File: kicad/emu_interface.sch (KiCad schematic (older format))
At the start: 19 parts

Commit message: power.sch added with new power 1V2, 3V3, an so global labels
I've added the power schematic and try to ojin the power label as 3V3,
VDD_3V3 an so.. keep going
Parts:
- C501, C504: renamed from C?; value ~ -> 4.7uF
- C503: renamed from C?; value ~ -> 0.01uF
- D502: renamed from D?; value ~ -> red
- D503: renamed from D?; value ~ -> blue
- D504: renamed from D?; value ~ -> green
- R501: renamed from R?; value ~ -> 680
- R502, R503: renamed from R?; value ~ -> 1.0k
- gave numbers to parts that had none: 10
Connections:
- net labels added: VDD_3V3
- net labels removed: VDD3V3

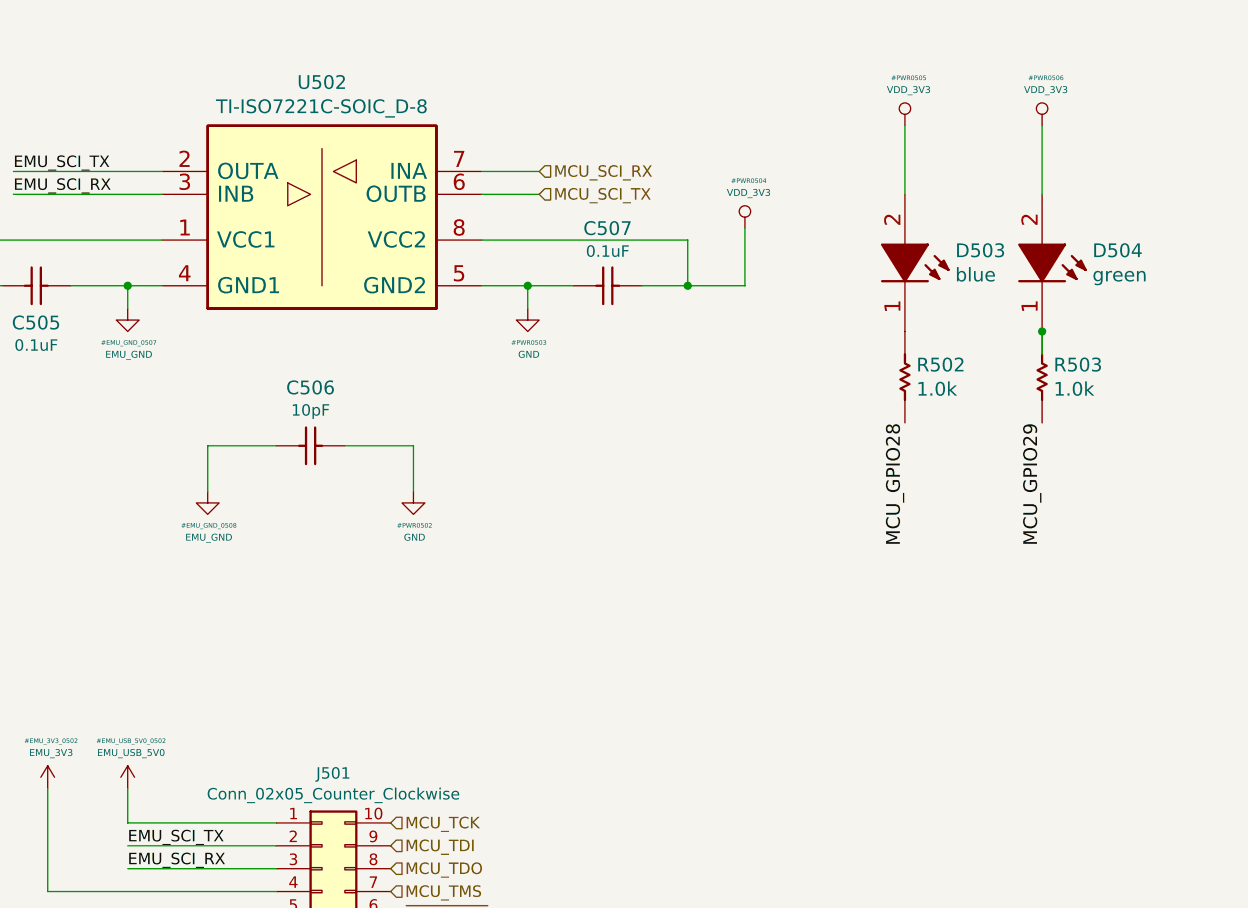
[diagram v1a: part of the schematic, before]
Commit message: clk.sch added. I'm seeing what to delete and what to keep
I've added clk.sch clk related schematics, so I'm looking to clean up
the design 'cose it has a lot of things not used in the actual design
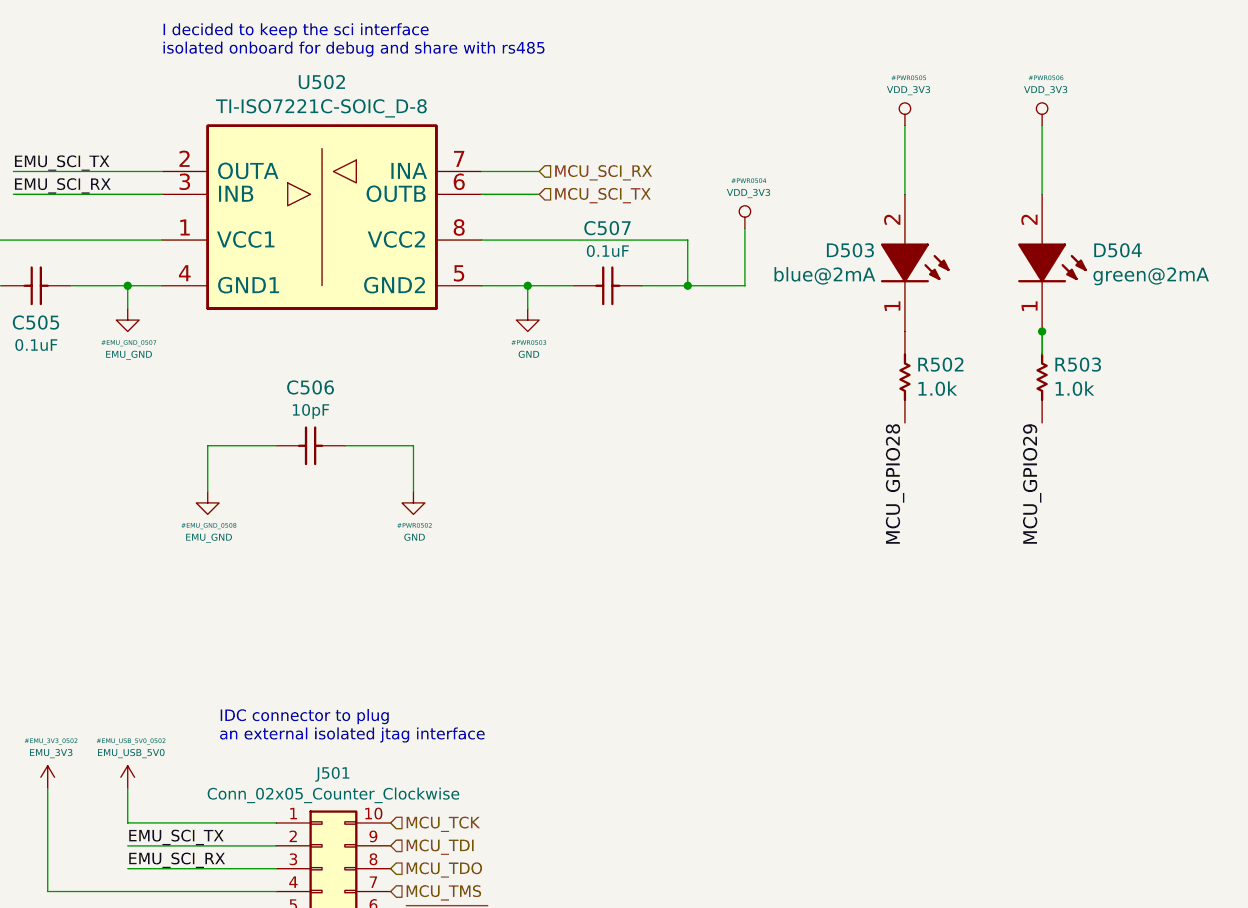
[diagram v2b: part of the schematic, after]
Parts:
- D503: VALUE blue -> blue@2mA
- D504: VALUE green -> green@2mA
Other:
- note added: "I decided to keep the sci interface \nisolated onboard for debug and share with rs485"
- note added: "IDC connector to plug \nan external isolated jtag interface"
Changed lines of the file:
@@
 $Descr B 17000 11000
 encoding utf-8
-Sheet 5 7
+Sheet 5 8
 Title "emu_interface"
 Date "25 10 2019"
-Rev ""
-Comp ""
-Comment1 ""
+Rev "1.0"
+Comp "dci"
+Comment1 "Pablo Slavkin"
 Comment2 ""
 Comment3 ""
@@
 F 2 "" H 13500 3550 50  0001 C CNN
 F 3 "" H 13500 3550 50  0001 C CNN
-F 4 "green" V 13553 3770 60  0000 L CNN "VALUE"
+F 4 "green@2mA" V 13553 3770 60  0000 L CNN "VALUE"
 	1    13500 3550
 	0    1    1    0
@@
 U 1 1 5DDA98EA
 P 12900 3550
-F 0 "D503" V 12847 3770 60  0000 L CNN
+F 0 "D503" V 12847 3421 60  0000 R CNN
 F 1 "blue" H 12900 3550 50  0001 C CNN
 F 2 "" H 12900 3550 50  0001 C CNN
 F 3 "" H 12900 3550 50  0001 C CNN
-F 4 "blue" V 12953 3770 60  0000 L CNN "VALUE"
+F 4 "blue@2mA" V 12953 3421 60  0000 R CNN "VALUE"
 	1    12900 3550
 	0    1    1    0
@@
 Text Label 9500 6200 0    50   ~ 0
 EMU_SCI_RX
+Text Notes 9900 5650 0    50   ~ 0
+IDC connector to plug \nan external isolated jtag interface
+Text Notes 9650 2650 0    50   ~ 0
+I decided to keep the sci interface \nisolated onboard for debug and share with rs485
 $EndSCHEMATC

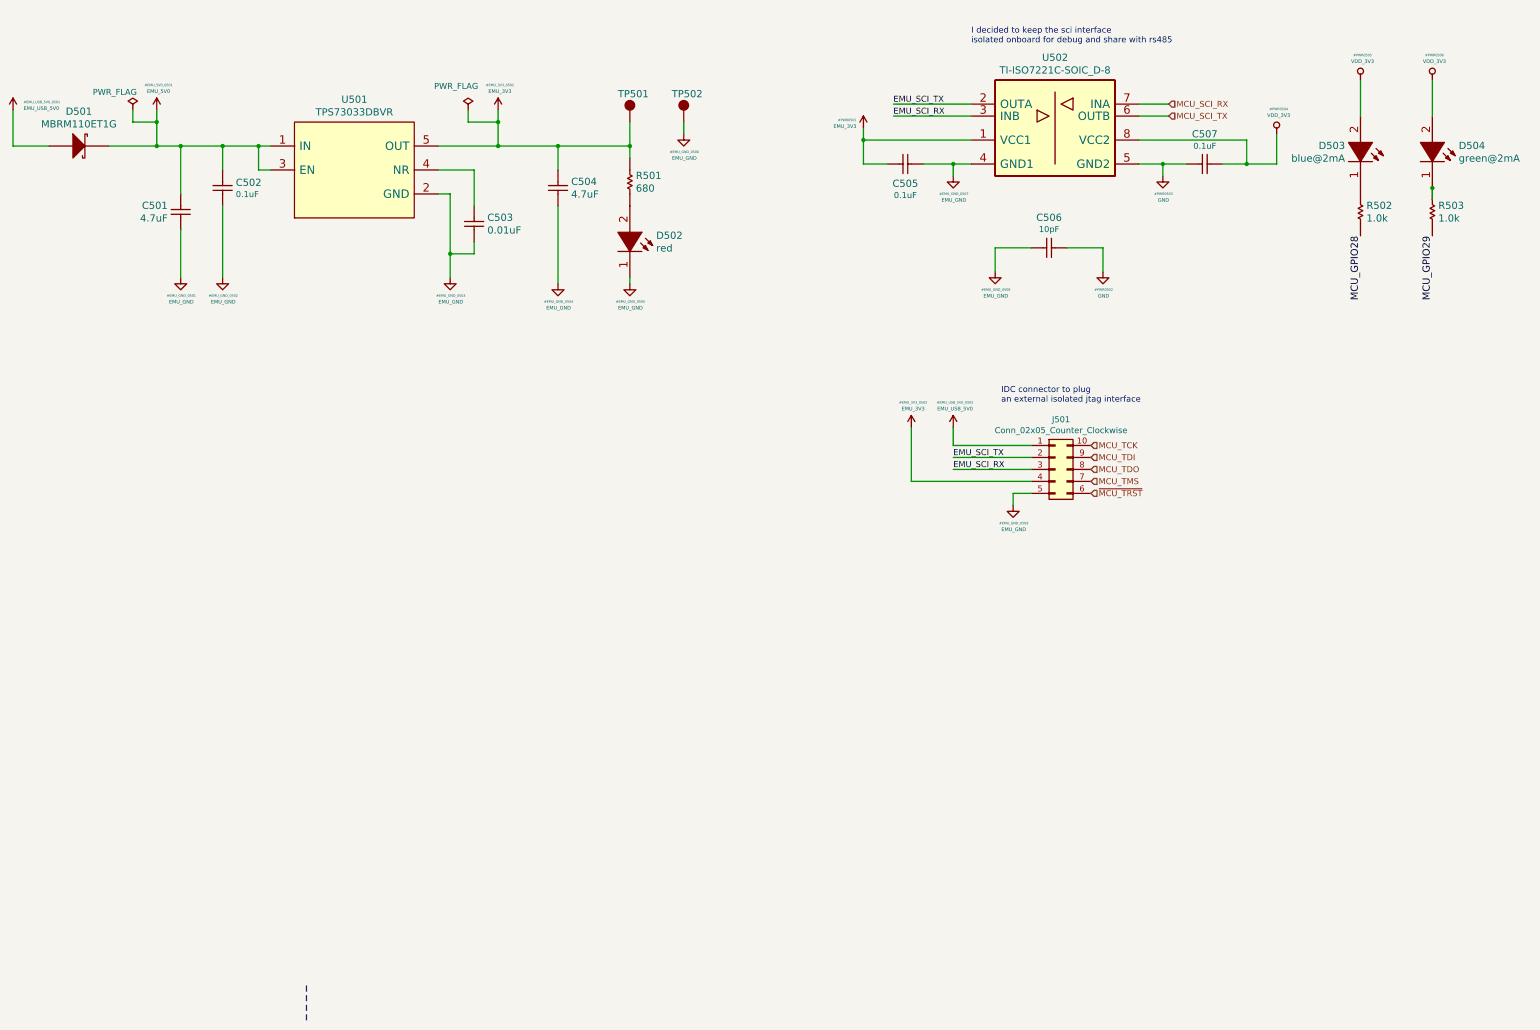
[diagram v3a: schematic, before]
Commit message: cleaning power, added ac/dc to 15v
I've added the ac/dc power supply based on encapsulated off load power
supply and chainde linear regulator for 5, 3v3 and 1v2 for cold gnd and
5v and 3v3 for hot gnd.
I'll next join some sheet 'cose some of those are almost empty
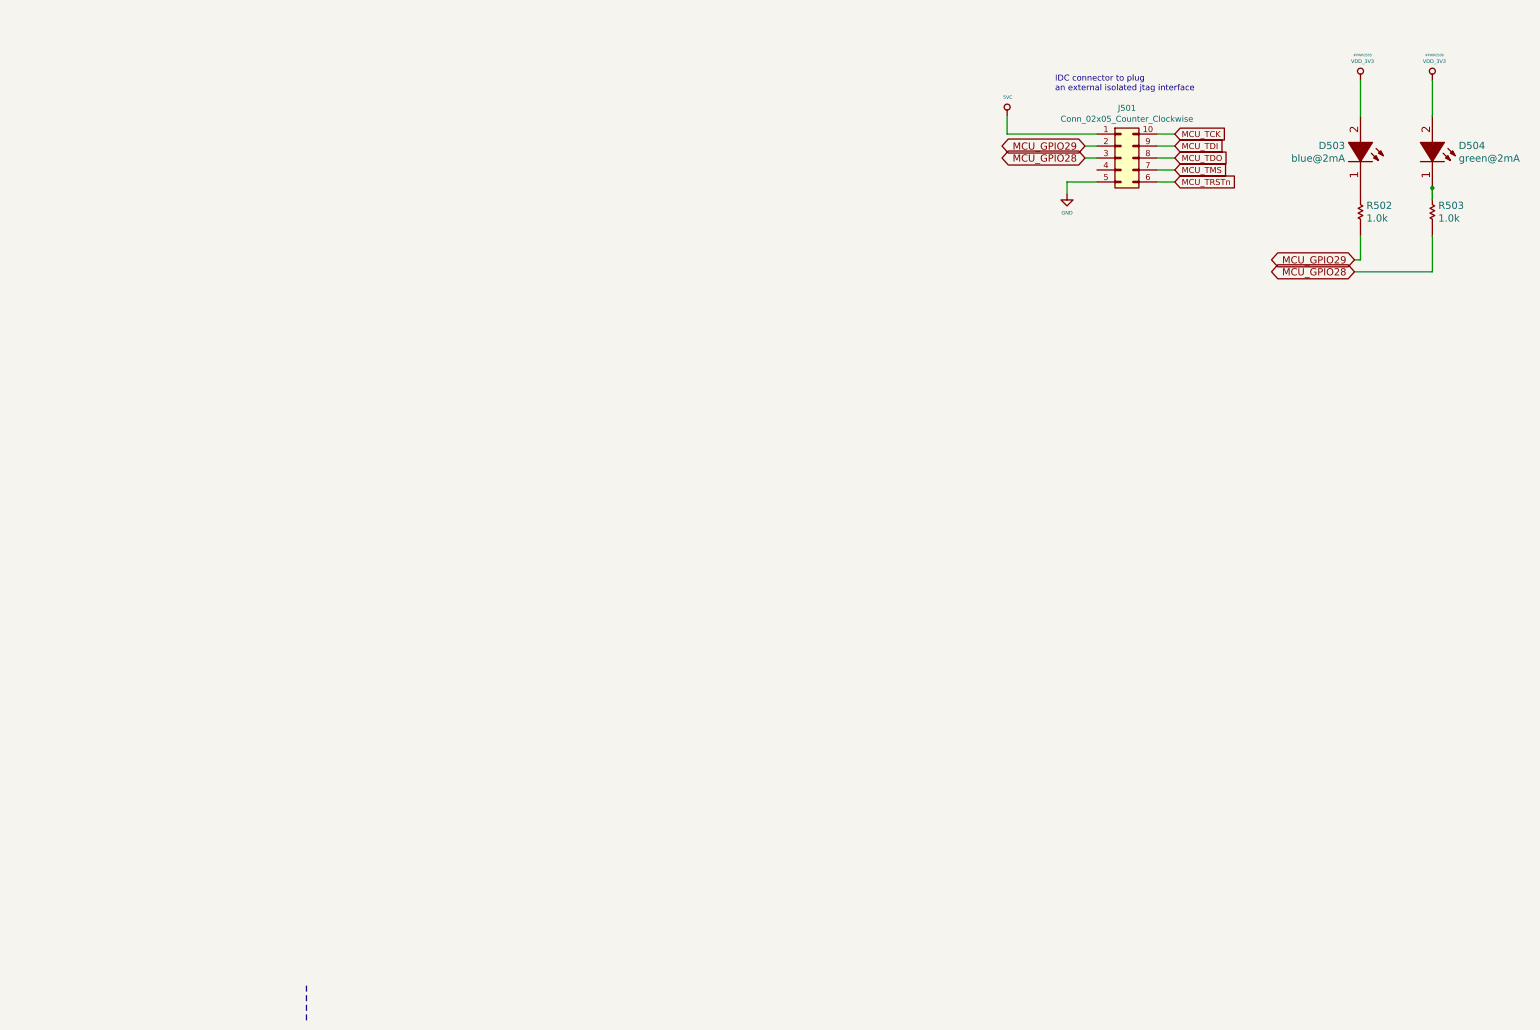
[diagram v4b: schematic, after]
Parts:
- removed C501, C504: 4.7uF, symbol servo:Capacitor
- removed C502, C505, C507: 0.1uF, symbol servo:Capacitor
- removed C503: 0.01uF, symbol servo:Capacitor
- removed C506: 10pF, symbol servo:Capacitor
- removed D501: MBRM110ET1G, symbol servo:DIODE_SCHOTTKY
- removed D502: red, symbol servo:LED_A2_K1
- removed R501: 680, symbol servo:Resistor
- removed TP501, TP502: ~, symbol servo:CMP-0078143-2
- removed U501: TPS73033DBVR, symbol servo:TPS730XXDBV
- removed U502: TI-ISO7221C-SOIC_D-8, symbol servo:TI-ISO7221C-SOIC_D-8
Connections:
- net labels added: 5VC, MCU_TRSTn
- net labels removed: EMU_3V3, EMU_5V0, EMU_GND, EMU_SCI_RX, EMU_SCI_TX, EMU_USB_5V0, MCU_SCI_RX, MCU_SCI_TX, ~MCU_TRST~
- wire segments 71 -> 18
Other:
- note removed: "I decided to keep the sci interface \nisolated onboard for debug and share with rs485"
- moved on the sheet: J501

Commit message: ok, it's enough cleaned to mix with power interface
I think it's time to mix with power interfaces.. It's enough cleaned
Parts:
- removed D503: blue, symbol servo:LED_A2_K1
- removed D504: green, symbol servo:LED_A2_K1
- removed J501: Conn_02x05_Counter_Clockwise, symbol Connector_Generic:Conn_02x05_Counter_Clockwise
- removed R502, R503: 1.0k, symbol servo:Resistor
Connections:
- net labels removed: 5VC, GND, MCU_GPIO28, MCU_GPIO29, MCU_TCK, MCU_TDI, MCU_TDO, MCU_TMS, MCU_TRSTn, VDD_3V3
- wire segments 18 -> 0
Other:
- note removed: "IDC connector to plug \nan external isolated jtag interface"
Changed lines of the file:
@@
 EESchema Schematic File Version 4
-LIBS:servo-cache
 EELAYER 26 0
 EELAYER END
-$Descr B 17000 11000
+$Descr A4 11693 8268
 encoding utf-8
-Sheet 5 9
-Title "emu_interface"
-Date "25 10 2019"
-Rev "1.0"
-Comp "dci"
-Comment1 "Pablo Slavkin"
+Sheet 1 9
+Title ""
+Date ""
+Rev ""
+Comp ""
+Comment1 ""
 Comment2 ""
 Comment3 ""
 Comment4 ""
 $EndDescr
-Wire Notes Line
-	4100 10800 4100 10500
-Wire Wire Line
-	12900 2950 12900 3250
-Wire Wire Line
-	13500 2950 13500 3250
-Wire Wire Line
-	13500 3850 13500 3950
-$Comp
-L servo:Resistor R?
-U 1 1 5DDA98D2
-P 12900 4050
-AR Path="/5DC1676A/5DDA98D2" Ref="R?"  Part="1"
-AR Path="/5DCD812E/5DDA98D2" Ref="R502"  Part="1"
-F 0 "R502" V 12847 4100 60  0000 L CNN
-F 1 "1.0k" H 12900 4050 50  0001 C CNN
-F 2 "" H 12900 4050 50  0001 C CNN
-F 3 "" H 12900 4050 50  0001 C CNN
-F 4 "1.0k" V 12953 4100 60  0000 L CNN "ValueDisplayed"
-	1    12900 4050
-	0    1    1    0
-$EndComp
-$Comp
-L servo:Resistor R?
-U 1 1 5DDA98DA
-P 13500 4050
-AR Path="/5DC1676A/5DDA98DA" Ref="R?"  Part="1"
-AR Path="/5DCD812E/5DDA98DA" Ref="R503"  Part="1"
-F 0 "R503" V 13447 4100 60  0000 L CNN
-F 1 "1.0k" H 13500 4050 50  0001 C CNN
-F 2 "" H 13500 4050 50  0001 C CNN
-F 3 "" H 13500 4050 50  0001 C CNN
-F 4 "1.0k" V 13553 4100 60  0000 L CNN "ValueDisplayed"
-	1    13500 4050
-	0    1    1    0
-$EndComp
-$Comp
-L servo:LED_A2_K1 D504
-U 1 1 5DDA98E2
-P 13500 3550
-F 0 "D504" V 13447 3770 60  0000 L CNN
-F 1 "green" H 13500 3550 50  0001 C CNN
-F 2 "" H 13500 3550 50  0001 C CNN
-F 3 "" H 13500 3550 50  0001 C CNN
-F 4 "green@2mA" V 13553 3770 60  0000 L CNN "VALUE"
-	1    13500 3550
-	0    1    1    0
-$EndComp
-$Comp
-L servo:LED_A2_K1 D503
-U 1 1 5DDA98EA
-P 12900 3550
-F 0 "D503" V 12847 3421 60  0000 R CNN
-F 1 "blue" H 12900 3550 50  0001 C CNN
-F 2 "" H 12900 3550 50  0001 C CNN
-F 3 "" H 12900 3550 50  0001 C CNN
-F 4 "blue@2mA" V 12953 3421 60  0000 R CNN "VALUE"
-	1    12900 3550
-	0    1    1    0
-$EndComp
-$Comp
-L servo:VDD_3V3 #PWR0505
-U 1 1 5DDAADCB
-P 12900 2950
-F 0 "#PWR0505" H 12917 3159 20  0000 C CNN
-F 1 "VDD_3V3" H 12917 3107 30  0000 C CNN
-F 2 "" H 12900 2950 70  0000 C CNN
-F 3 "" H 12900 2950 70  0000 C CNN
-	1    12900 2950
-	1    0    0    -1
-$EndComp
-$Comp
-L servo:VDD_3V3 #PWR0506
-U 1 1 5DDAAF80
-P 13500 2950
-F 0 "#PWR0506" H 13517 3159 20  0000 C CNN
-F 1 "VDD_3V3" H 13517 3107 30  0000 C CNN
-F 2 "" H 13500 2950 70  0000 C CNN
-F 3 "" H 13500 2950 70  0000 C CNN
-	1    13500 2950
-	1    0    0    -1
-$EndComp
-Connection ~ 13500 3850
-$Comp
-L Connector_Generic:Conn_02x05_Counter_Clockwise J501
-U 1 1 5DD48AB5
-P 10900 3600
-F 0 "J501" H 10950 4017 50  0000 C CNN
-F 1 "Conn_02x05_Counter_Clockwise" H 10950 3926 50  0000 C CNN
-F 2 "" H 10900 3600 50  0001 C CNN
-F 3 "~" H 10900 3600 50  0001 C CNN
-	1    10900 3600
-	1    0    0    -1
-$EndComp
-Wire Wire Line
-	10700 3400 9950 3400
-Wire Wire Line
-	9950 3400 9950 3250
-Wire Wire Line
-	10700 3800 10450 3800
-Wire Wire Line
-	10450 3800 10450 3900
-Text Notes 10350 3050 0    50   ~ 0
-IDC connector to plug \nan external isolated jtag interface
-Text GLabel 11350 3400 2    50   Input ~ 0
-MCU_TCK
-Text GLabel 11350 3600 2    50   Input ~ 0
-MCU_TDO
-Text GLabel 11350 3500 2    50   Input ~ 0
-MCU_TDI
-Text GLabel 11350 3800 2    50   Input ~ 0
-MCU_TRSTn
-Text GLabel 11350 3700 2    50   Input ~ 0
-MCU_TMS
-Wire Wire Line
-	11350 3400 11200 3400
-Wire Wire Line
-	11200 3500 11350 3500
-Wire Wire Line
-	11350 3600 11200 3600
-Wire Wire Line
-	11200 3700 11350 3700
-Wire Wire Line
-	11350 3800 11200 3800
-Text GLabel 12850 4450 0    60   BiDi ~ 0
-MCU_GPIO29
-Text GLabel 12850 4550 0    60   BiDi ~ 0
-MCU_GPIO28
-Wire Wire Line
-	10700 3600 10600 3600
-Wire Wire Line
-	10600 3500 10700 3500
-Wire Wire Line
-	12850 4450 12900 4450
-Wire Wire Line
-	12900 4450 12900 4250
-Wire Wire Line
-	12850 4550 13500 4550
-Wire Wire Line
-	13500 4550 13500 4250
-Text GLabel 10600 3500 0    60   BiDi ~ 0
-MCU_GPIO29
-Text GLabel 10600 3600 0    60   BiDi ~ 0
-MCU_GPIO28
-$Comp
-L servo:5VC #PWR?
-U 1 1 5DE432F9
-P 9950 3250
-AR Path="/5DD76B18/5DE432F9" Ref="#PWR?"  Part="1"
-AR Path="/5DCD812E/5DE432F9" Ref="#PWR?"  Part="1"
-F 0 "#PWR?" H 9950 3050 20  0001 C CNN
-F 1 "5VC" H 9955 3407 28  0000 C CNN
-F 2 "" H 9950 3250 50  0001 C CNN
-F 3 "" H 9950 3250 50  0001 C CNN
-	1    9950 3250
-	1    0    0    -1
-$EndComp
-$Comp
-L servo:GND #PWR?
-U 1 1 5DE44EE9
-P 10450 3900
-F 0 "#PWR?" H 10450 3650 30  0001 C CNN
-F 1 "GND" H 10450 3742 30  0000 C CNN
-F 2 "" H 10450 3900 50  0001 C CNN
-F 3 "" H 10450 3900 50  0001 C CNN
-	1    10450 3900
-	1    0    0    -1
-$EndComp
 $EndSCHEMATC
